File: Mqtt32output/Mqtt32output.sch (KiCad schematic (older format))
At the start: 24 parts, among them J1 OUTPUT 0-7, J2 OUTPUT 8-15, J3 OUTPUT 16-23, J4 OUTPUT 24-31, SW1 DIP SWITCH NODE NUMBER 0..3, U2 74HC595, U4 74HC595, U6 74HC595, U8 74HC595, X1 0V - 5V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

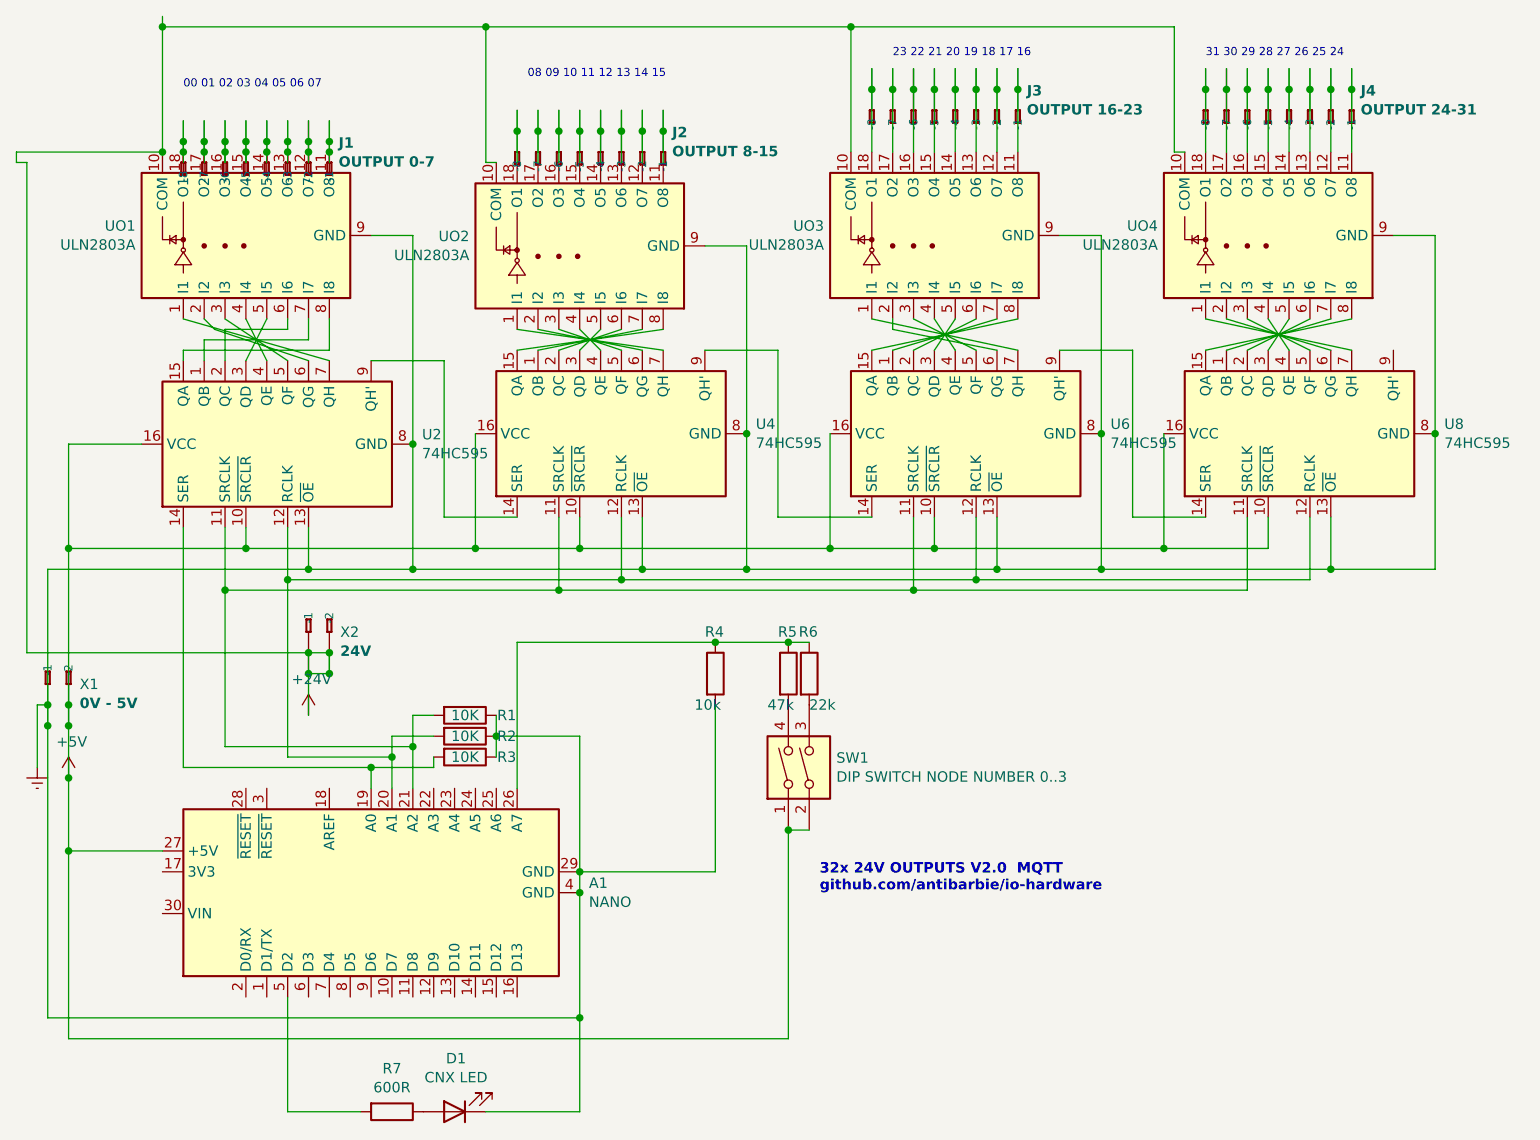
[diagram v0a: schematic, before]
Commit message: Fix component placement, and GND connexion + board size on inputs
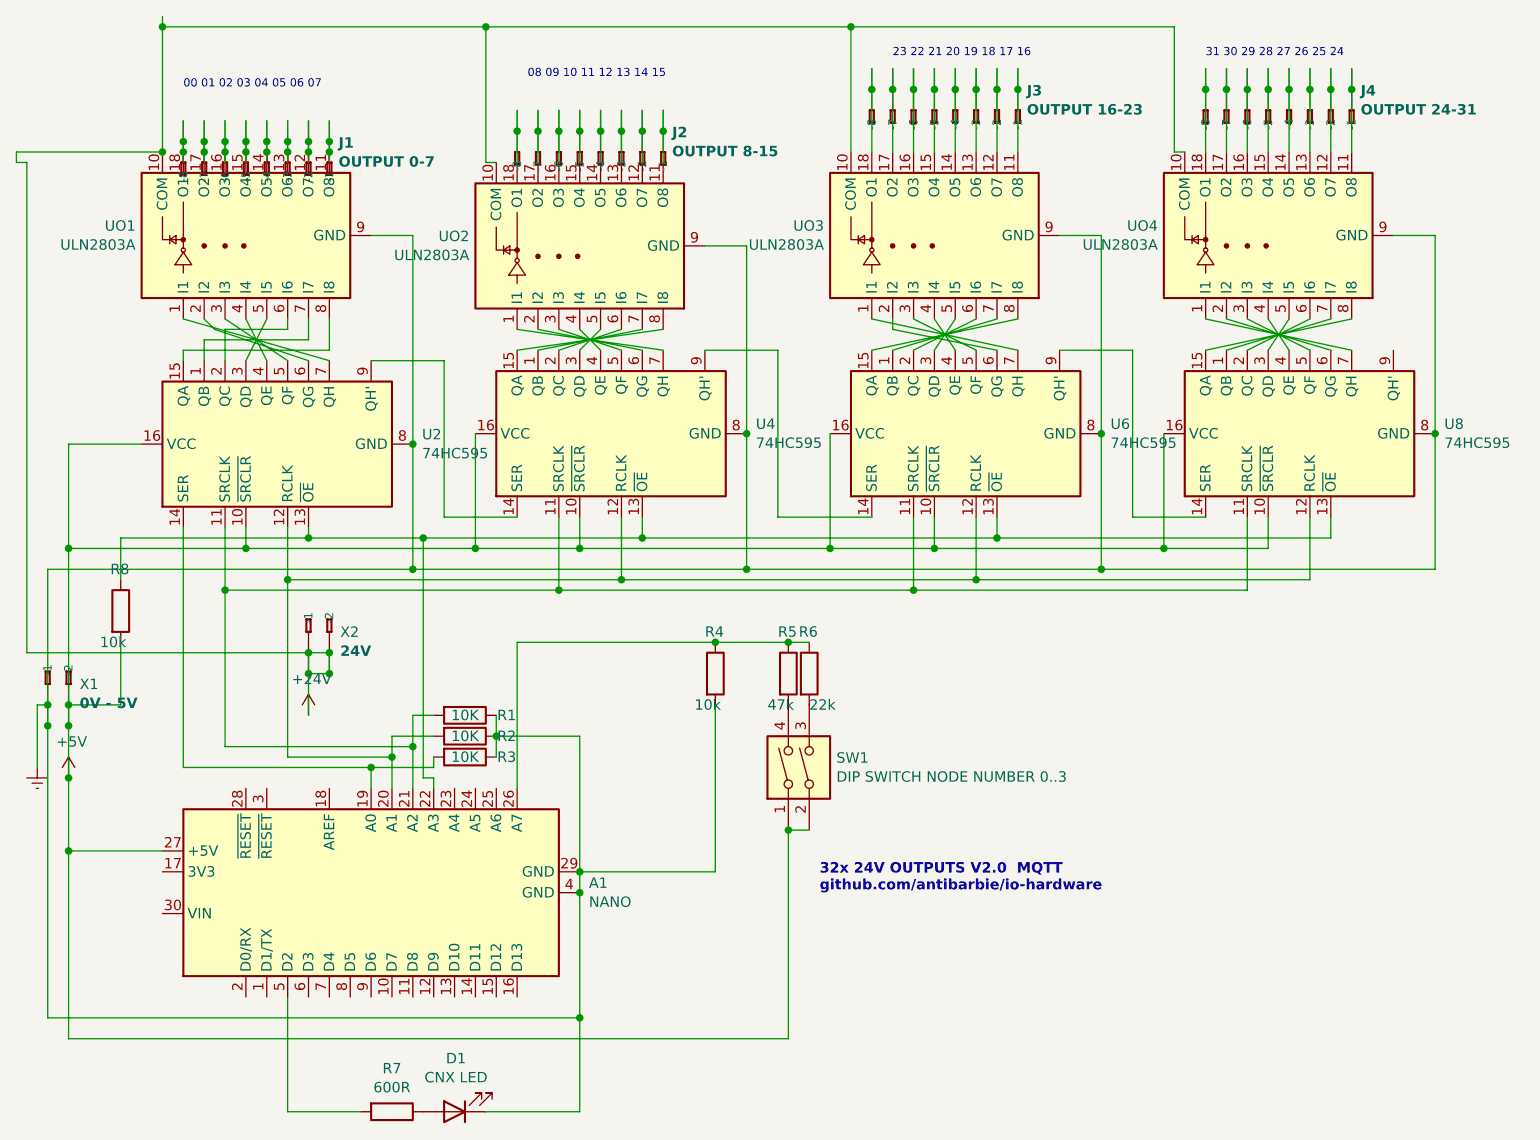
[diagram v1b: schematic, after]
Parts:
- added R8: 10k, Resistor_THT:R_Axial_DIN0207_L6.3mm_D2.5mm_P2.54mm_Vertical, symbol Device:R
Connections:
- wire segments 241 -> 248
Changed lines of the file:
@@
 	1300 3900 1300 3250
-Wire Wire Line
-	1300 3250 2550 3250
 Wire Wire Line
 	3050 3250 3050 2650
@@
 Wire Wire Line
 	4650 1700 4650 2600
-Wire Wire Line
-	4650 3250 4150 3250
 Connection ~ 3050 3250
 Wire Wire Line
@@
 Wire Wire Line
 	6350 2600 6350 3250
-Wire Wire Line
-	6350 3250 5850 3250
 Connection ~ 6350 2600
 Connection ~ 4650 3250
@@
 Wire Wire Line
 	7950 2600 7950 3250
-Wire Wire Line
-	7950 3250 7450 3250
 Connection ~ 7950 2600
 Connection ~ 6350 3250
@@
 Wire Wire Line
 	2250 3150 3350 3150
-Wire Wire Line
-	2550 3250 2550 3050
-Connection ~ 2550 3250
-Wire Wire Line
-	2550 3250 3050 3250
-Wire Wire Line
-	4150 3250 4150 3000
-Connection ~ 4150 3250
-Wire Wire Line
-	4150 3250 3050 3250
-Wire Wire Line
-	5850 3250 5850 3000
-Connection ~ 5850 3250
-Wire Wire Line
-	5850 3250 4650 3250
-Wire Wire Line
-	7450 3250 7450 3000
-Connection ~ 7450 3250
-Wire Wire Line
-	7450 3250 6350 3250
 Wire Wire Line
 	3400 650  3400 1300
@@
 	3850 5850 3850 5400
 Connection ~ 3850 5400
+Wire Wire Line
+	6350 3250 7950 3250
+Wire Wire Line
+	4650 3250 6350 3250
+Wire Wire Line
+	3050 3250 4650 3250
+Wire Wire Line
+	1300 3250 3050 3250
+Wire Wire Line
+	2550 3050 2550 3100
+Wire Wire Line
+	2550 3100 3100 3100
+Wire Wire Line
+	4150 3100 4150 3000
+Wire Wire Line
+	4150 3100 5850 3100
+Wire Wire Line
+	5850 3100 5850 3000
+Connection ~ 4150 3100
+Wire Wire Line
+	5850 3100 7450 3100
+Wire Wire Line
+	7450 3100 7450 3000
+Connection ~ 5850 3100
+Wire Wire Line
+	3150 4300 3150 4250
+Wire Wire Line
+	3150 4250 3100 4250
+Wire Wire Line
+	3100 4250 3100 3100
+Connection ~ 3100 3100
+Wire Wire Line
+	3100 3100 4150 3100
+$Comp
+L Device:R R8
+U 1 1 5FDDFDC2
+P 1650 3450
+F 0 "R8" H 1600 3650 50  0000 L CNN
+F 1 "10k" H 1550 3300 50  0000 L CNN
+F 2 "Resistor_THT:R_Axial_DIN0207_L6.3mm_D2.5mm_P2.54mm_Vertical" V 1580 3450 50  0001 C CNN
+F 3 "~" H 1650 3450 50  0001 C CNN
+	1    1650 3450
+	1    0    0    -1
+$EndComp
+Wire Wire Line
+	1400 3900 1650 3900
+Wire Wire Line
+	1650 3900 1650 3600
+Wire Wire Line
+	1650 3300 1650 3100
+Wire Wire Line
+	1650 3100 2550 3100
+Connection ~ 2550 3100
 $EndSCHEMATC
